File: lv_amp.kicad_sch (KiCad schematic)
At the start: 79 parts, among them J1 Jack-DC, J2 AudioJack2, J3 AudioJack2, Q1 Q_NMOS_DGS, U1 MAX1771xSA, U2 TL072, U3 ECC83, U4 ECC83, U5 ECC83

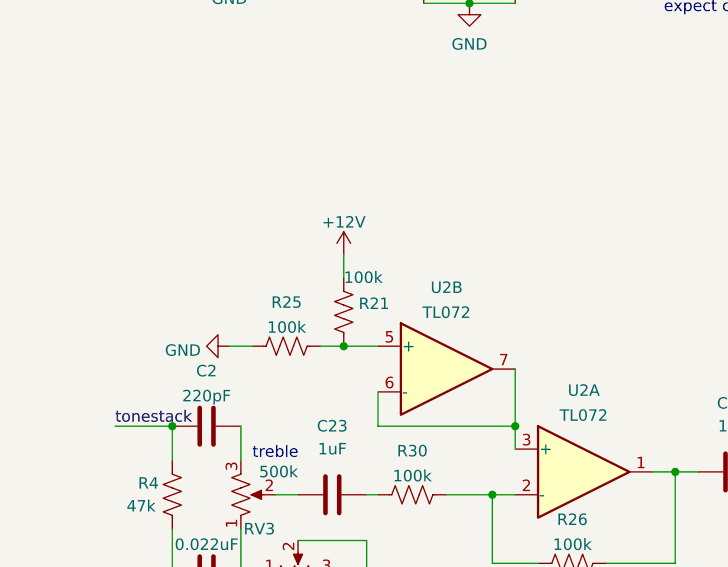
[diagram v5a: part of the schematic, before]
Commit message: alpha0 errata: dd zener diode to output reference
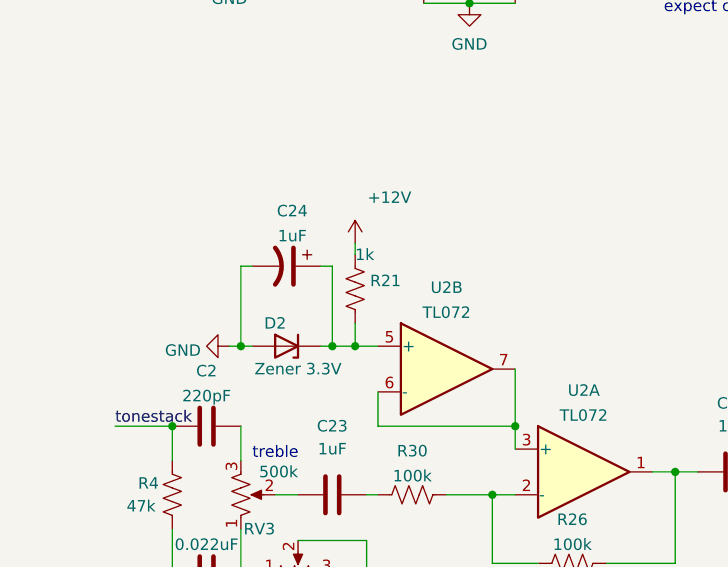
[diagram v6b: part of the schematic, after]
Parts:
- removed R25: 100k, Resistor_SMD:R_0603_1608Metric, symbol Device:R_US
- added C24: 1uF, Capacitor_SMD:CP_Elec_4x5.4, symbol Device:C_Polarized_US
- added D2: Zener 3.3V, Diode_SMD:D_SOT-23_ANK, symbol Device:D_Zener
- R21: value 100k -> 1k
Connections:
- net GND: now also C24.2, D2.2 (A)
- net at R21.2, U2.5 (+): now also C24.1, D2.1 (K)
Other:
- moved on the sheet: R21
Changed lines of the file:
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@@
 (kicad_sch (version 20211123) (generator eeschema)
   (paper "A4")
+  (junction (at 36.83 143.51) (diameter 0) (color 0 0 0 0)
+  )
   (junction (at 115.57 96.52) (diameter 0) (color 0 0 0 0)
   )
@@
   (junction (at 85.09 157.48) (diameter 0) (color 0 0 0 0)
   )
-  (junction (at 48.26 143.51) (diameter 0) (color 0 0 0 0)
+  (junction (at 49.53 143.51) (diameter 0) (color 0 0 0 0)
   )
   (junction (at 222.25 80.01) (diameter 0) (color 0 0 0 0)
@@
   (junction (at 139.7 82.55) (diameter 0) (color 0 0 0 0)
   )
+  (junction (at 46.99 143.51) (diameter 0) (color 0 0 0 0)
+  )
   (junction (at 124.46 139.7) (diameter 0) (color 0 0 0 0)
   )
@@
   (no_connect (at 110.49 160.02))
   (no_connect (at 110.49 154.94))
-  (wire (pts (xy 45.72 143.51) (xy 48.26 143.51))
+  (wire (pts (xy 45.72 143.51) (xy 46.99 143.51))
     (stroke (width 0) (type default) (color 0 0 0 0))
   )
@@
     (stroke (width 0) (type default) (color 0 0 0 0))
   )
+  (wire (pts (xy 36.83 134.62) (xy 36.83 143.51))
+    (stroke (width 0) (type default) (color 0 0 0 0))
+  )
   (wire (pts (xy 95.25 157.48) (xy 99.06 157.48))
     (stroke (width 0) (type default) (color 0 0 0 0))
@@
     (stroke (width 0) (type default) (color 0 0 0 0))
   )
+  (wire (pts (xy 36.83 143.51) (xy 38.1 143.51))
+    (stroke (width 0) (type default) (color 0 0 0 0))
+  )
   (wire (pts (xy 194.31 119.38) (xy 198.12 119.38))
     (stroke (width 0) (type default) (color 0 0 0 0))
@@
     (stroke (width 0) (type default) (color 0 0 0 0))
   )
+  (wire (pts (xy 46.99 143.51) (xy 49.53 143.51))
+    (stroke (width 0) (type default) (color 0 0 0 0))
+  )
   (wire (pts (xy 152.4 92.71) (xy 152.4 95.25))
     (stroke (width 0) (type default) (color 0 0 0 0))
@@
     (stroke (width 0) (type default) (color 0 0 0 0))
   )
+  (wire (pts (xy 45.72 134.62) (xy 46.99 134.62))
+    (stroke (width 0) (type default) (color 0 0 0 0))
+  )
   (wire (pts (xy 107.95 152.4) (xy 110.49 152.4))
     (stroke (width 0) (type default) (color 0 0 0 0))
@@
     (stroke (width 0) (type default) (color 0 0 0 0))
   )
+  (wire (pts (xy 46.99 134.62) (xy 46.99 143.51))
+    (stroke (width 0) (type default) (color 0 0 0 0))
+  )
   (wire (pts (xy 43.18 185.42) (xy 43.18 190.5))
     (stroke (width 0) (type default) (color 0 0 0 0))
@@
     (stroke (width 0) (type default) (color 0 0 0 0))
   )
-  (wire (pts (xy 48.26 143.51) (xy 52.07 143.51))
+  (wire (pts (xy 49.53 143.51) (xy 52.07 143.51))
     (stroke (width 0) (type default) (color 0 0 0 0))
   )
@@
     (stroke (width 0) (type default) (color 0 0 0 0))
   )
-  (wire (pts (xy 48.26 133.35) (xy 48.26 135.89))
+  (wire (pts (xy 29.21 168.91) (xy 29.21 181.61))
     (stroke (width 0) (type default) (color 0 0 0 0))
   )
-  (wire (pts (xy 29.21 168.91) (xy 29.21 181.61))
+  (wire (pts (xy 49.53 140.97) (xy 49.53 143.51))
     (stroke (width 0) (type default) (color 0 0 0 0))
   )
@@
     (stroke (width 0) (type default) (color 0 0 0 0))
   )
+  (wire (pts (xy 38.1 134.62) (xy 36.83 134.62))
+    (stroke (width 0) (type default) (color 0 0 0 0))
+  )
   (wire (pts (xy 203.2 119.38) (xy 203.2 121.92))
     (stroke (width 0) (type default) (color 0 0 0 0))
@@
     (stroke (width 0) (type default) (color 0 0 0 0))
   )
-  (wire (pts (xy 35.56 143.51) (xy 38.1 143.51))
+  (wire (pts (xy 35.56 143.51) (xy 36.83 143.51))
     (stroke (width 0) (type default) (color 0 0 0 0))
   )
@@
     (stroke (width 0) (type default) (color 0 0 0 0))
   )
+  (wire (pts (xy 49.53 133.35) (xy 49.53 132.08))
+    (stroke (width 0) (type default) (color 0 0 0 0))
+  )
   (wire (pts (xy 139.7 96.52) (xy 139.7 99.06))
     (stroke (width 0) (type default) (color 0 0 0 0))
@@
     (pin "1")
   )
+  (symbol (lib_id "Device:C_Polarized_US") (at 41.91 134.62 270) (unit 1)
+    (in_bom yes) (on_board yes) (fields_autoplaced)
+    (property "Reference" "C24" (id 0) (at 42.545 128.4945 90))
+    (property "Value" "1uF" (id 1) (at 42.545 131.2696 90))
+    (property "Footprint" "Capacitor_SMD:CP_Elec_4x5.4" (id 2) (at 41.91 134.62 0)
+      (effects (font (size 1.27 1.27)) hide)
+    )
+    (property "Datasheet" "~" (id 3) (at 41.91 134.62 0)
+      (effects (font (size 1.27 1.27)) hide)
+    )
+    (pin "1")
+    (pin "2")
+  )
   (symbol (lib_id "power:PWR_FLAG") (at 109.22 119.38 180) (unit 1)
     (in_bom yes) (on_board yes) (fields_autoplaced)
@@
     (pin "1")
   )
-  (symbol (lib_id "Device:R_US") (at 41.91 143.51 90) (unit 1)
-    (in_bom yes) (on_board yes) (fields_autoplaced)
-    (property "Reference" "R25" (id 0) (at 41.91 138.6545 90))
-    (property "Value" "100k" (id 1) (at 41.91 141.4296 90))
-    (property "Footprint" "Resistor_SMD:R_0603_1608Metric" (id 2) (at 42.164 142.494 90)
-      (effects (font (size 1.27 1.27)) hide)
-    )
-    (property "Datasheet" "~" (id 3) (at 41.91 143.51 0)
-      (effects (font (size 1.27 1.27)) hide)
-    )
-    (pin "1")
-    (pin "2")
-  )
-  (symbol (lib_id "power:+12V") (at 48.26 133.35 0) (unit 1)
-    (in_bom yes) (on_board yes) (fields_autoplaced)
-    (property "Reference" "#PWR05" (id 0) (at 48.26 137.16 0)
+  (symbol (lib_id "power:+12V") (at 49.53 132.08 0) (unit 1)
+    (in_bom yes) (on_board yes)
+    (property "Reference" "#PWR05" (id 0) (at 49.53 135.89 0)
       (effects (font (size 1.27 1.27)) hide)
     )
-    (property "Value" "+12V" (id 1) (at 48.26 129.7455 0))
-    (property "Footprint" "" (id 2) (at 48.26 133.35 0)
+    (property "Value" "+12V" (id 1) (at 53.34 127 0))
+    (property "Footprint" "" (id 2) (at 49.53 132.08 0)
       (effects (font (size 1.27 1.27)) hide)
     )
-    (property "Datasheet" "" (id 3) (at 48.26 133.35 0)
+    (property "Datasheet" "" (id 3) (at 49.53 132.08 0)
       (effects (font (size 1.27 1.27)) hide)
     )
@@
     (pin "8")
   )
+  (symbol (lib_id "Device:D_Zener") (at 41.91 143.51 180) (unit 1)
+    (in_bom yes) (on_board yes)
+    (property "Reference" "D2" (id 0) (at 40.64 140.97 0))
+    (property "Value" "Zener 3.3V" (id 1) (at 43.18 146.05 0))
+    (property "Footprint" "Diode_SMD:D_SOT-23_ANK" (id 2) (at 41.91 143.51 0)
+      (effects (font (size 1.27 1.27)) hide)
+    )
+    (property "Datasheet" "~" (id 3) (at 41.91 143.51 0)
+      (effects (font (size 1.27 1.27)) hide)
+    )
+    (pin "1")
+    (pin "2")
+  )
   (symbol (lib_id "power:HT") (at 154.94 57.15 0) (unit 1)
     (in_bom yes) (on_board yes) (fields_autoplaced)
@@
     (pin "1")
   )
-  (symbol (lib_id "Device:R_US") (at 48.26 139.7 0) (unit 1)
+  (symbol (lib_id "Device:R_US") (at 49.53 137.16 0) (unit 1)
     (in_bom yes) (on_board yes)
-    (property "Reference" "R21" (id 0) (at 49.911 138.7915 0)
+    (property "Reference" "R21" (id 0) (at 51.181 136.2515 0)
       (effects (font (size 1.27 1.27)) (justify left))
     )
-    (property "Value" "100k" (id 1) (at 48.26 135.89 0)
+    (property "Value" "1k" (id 1) (at 49.53 133.35 0)
       (effects (font (size 1.27 1.27)) (justify left))
     )
-    (property "Footprint" "Resistor_SMD:R_0603_1608Metric" (id 2) (at 49.276 139.954 90)
+    (property "Footprint" "Resistor_SMD:R_0603_1608Metric" (id 2) (at 50.546 137.414 90)
       (effects (font (size 1.27 1.27)) hide)
     )
-    (property "Datasheet" "~" (id 3) (at 48.26 139.7 0)
+    (property "Datasheet" "~" (id 3) (at 49.53 137.16 0)
       (effects (font (size 1.27 1.27)) hide)
     )
@@
       (reference "C23") (unit 1) (value "1uF") (footprint "Capacitor_THT:C_Rect_L18.0mm_W7.0mm_P15.00mm_FKS3_FKP3")
     )
+    (path "/1dea0fc0-4f42-491f-9959-2b5fca8108e3"
+      (reference "C24") (unit 1) (value "1uF") (footprint "Capacitor_SMD:CP_Elec_4x5.4")
+    )
     (path "/3b57d871-c725-4716-ad9b-2bb76745f388"
       (reference "D1") (unit 1) (value "D") (footprint "Package_TO_SOT_SMD:TO-263-2_TabPin1")
     )
+    (path "/d46bdf2a-1124-4fea-af8f-34f8f4677f71"
+      (reference "D2") (unit 1) (value "Zener 3.3V") (footprint "Diode_SMD:D_SOT-23_ANK")
+    )
     (path "/2f758966-b33c-4bfa-a976-e7af6b3674c7"
       (reference "H1") (unit 1) (value "MountingHole_Pad") (footprint "MountingHole:MountingHole_3.2mm_M3")
@@
     )
     (path "/de2cc584-d34c-40e4-994c-f25e00753375"
-      (reference "R21") (unit 1) (value "100k") (footprint "Resistor_SMD:R_0603_1608Metric")
+      (reference "R21") (unit 1) (value "1k") (footprint "Resistor_SMD:R_0603_1608Metric")
     )
     (path "/85a0f53d-b7a0-471e-8040-11e73cdeb82b"
@@
       (reference "R24") (unit 1) (value "68k") (footprint "Resistor_SMD:R_0603_1608Metric")
     )
-    (path "/8a00be0e-0422-46b1-bc29-f9a0713039c2"
-      (reference "R25") (unit 1) (value "100k") (footprint "Resistor_SMD:R_0603_1608Metric")
-    )
     (path "/413fa014-254c-4b9e-a537-06e0dc8d85fa"

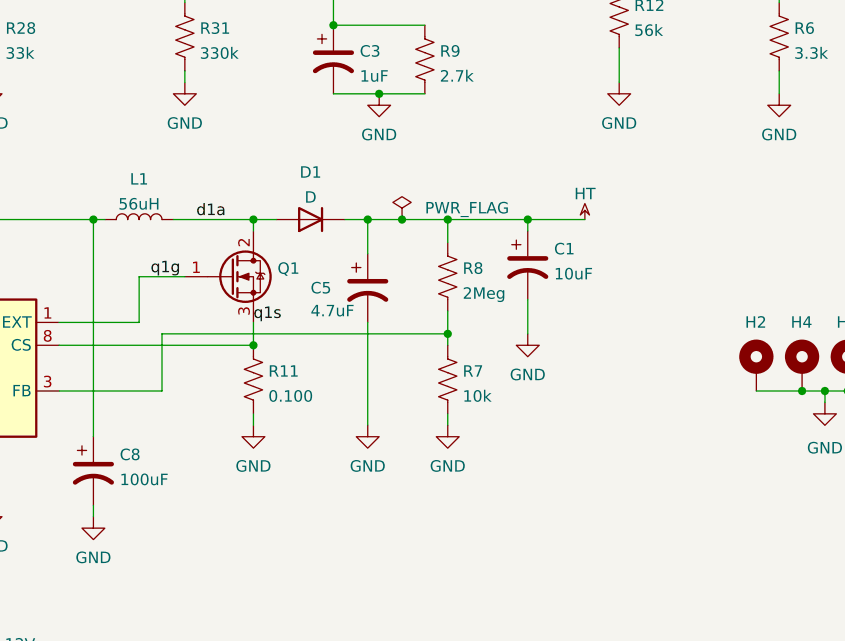
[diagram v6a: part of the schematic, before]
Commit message: alpha0 errata: better output filtering on supply
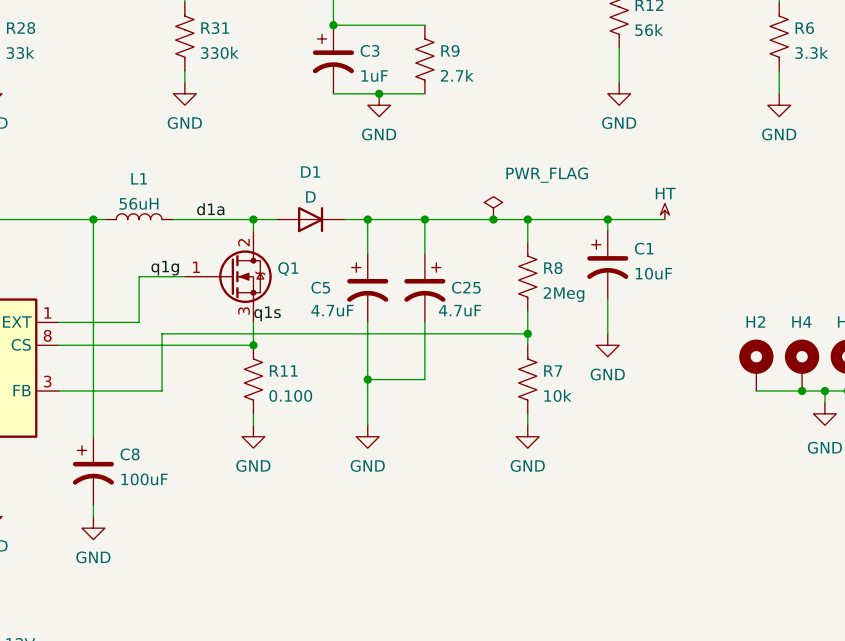
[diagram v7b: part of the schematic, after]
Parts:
- added C25: 4.7uF, Capacitor_SMD:CP_Elec_10x10, symbol Device:C_Polarized_US
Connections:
- net GND: now also C25.2
- net HT: now also C25.1
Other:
- moved on the sheet: C1, R7, R8
